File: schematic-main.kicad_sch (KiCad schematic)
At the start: 14 parts, among them J1 Conn_01x02, J2 Conn_01x03, J3 Conn_01x03_Pin, J6 Conn_01x04, P1 USB_C_Plug_USB2.0

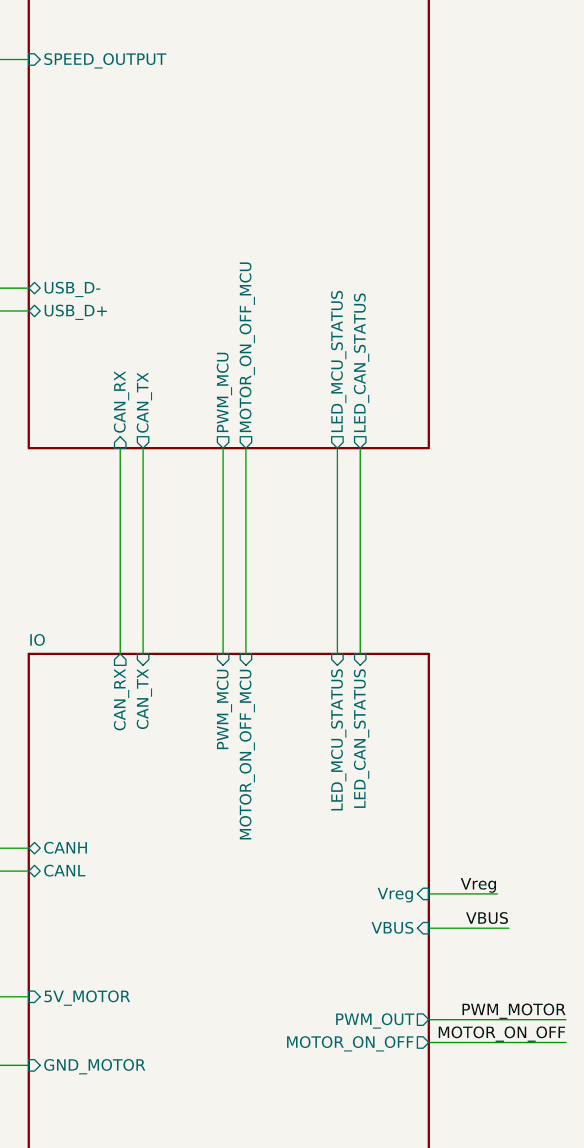
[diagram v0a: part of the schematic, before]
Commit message: Add test pins for I/O MCU
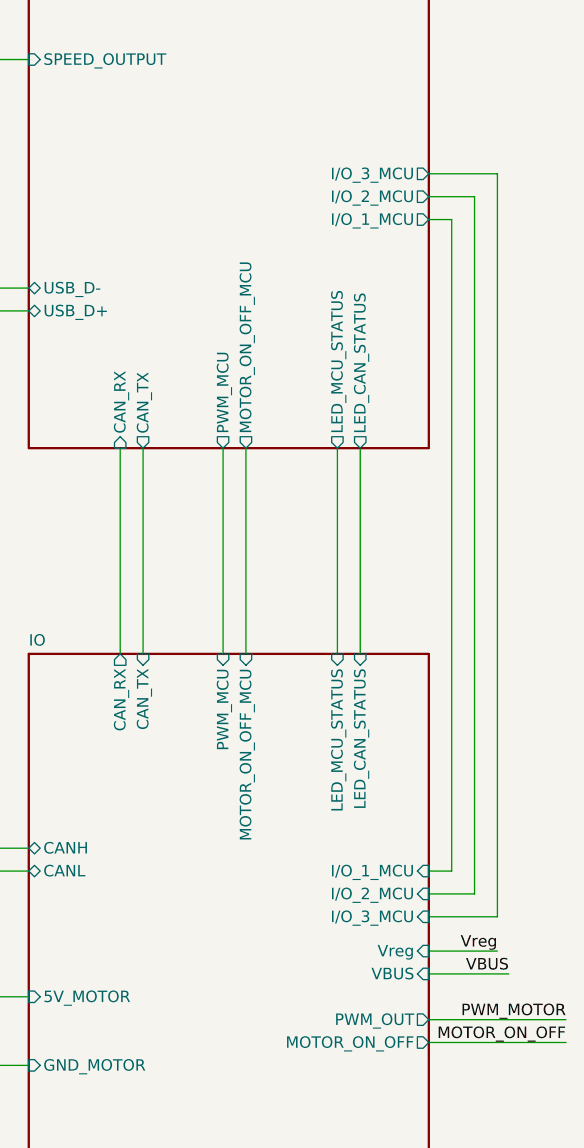
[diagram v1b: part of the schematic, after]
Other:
- sheet IO ports: added I/O_1_MCU, I/O_2_MCU, I/O_3_MCU; removed none
- sheet MCU ports: added I/O_1_MCU, I/O_2_MCU, I/O_3_MCU; removed none
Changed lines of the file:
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@@
     (stroke (width 0) (type default))
   )
-  (wire (pts (xy 179.07 134.62) (xy 187.96 134.62))
+  (wire (pts (xy 179.07 139.7) (xy 187.96 139.7))
+    (stroke (width 0) (type default))
+  )
+  (wire (pts (xy 179.07 130.81) (xy 184.15 130.81))
     (stroke (width 0) (type default))
   )
@@
     (stroke (width 0) (type default))
   )
+  (wire (pts (xy 186.69 50.8) (xy 186.69 133.35))
+    (stroke (width 0) (type default))
+  )
+  (wire (pts (xy 184.15 130.81) (xy 184.15 53.34))
+    (stroke (width 0) (type default))
+  )
   (wire (pts (xy 156.21 81.28) (xy 156.21 104.14))
     (stroke (width 0) (type default))
@@
     (stroke (width 0) (type default))
   )
-  (wire (pts (xy 179.07 130.81) (xy 186.69 130.81))
+  (wire (pts (xy 179.07 137.16) (xy 186.69 137.16))
     (stroke (width 0) (type default))
   )
@@
     (stroke (width 0) (type default))
   )
+  (wire (pts (xy 181.61 128.27) (xy 179.07 128.27))
+    (stroke (width 0) (type default))
+  )
   (wire (pts (xy 54.61 35.56) (xy 60.96 35.56))
     (stroke (width 0) (type default))
   )
+  (wire (pts (xy 179.07 53.34) (xy 184.15 53.34))
+    (stroke (width 0) (type default))
+  )
   (wire (pts (xy 130.81 147.32) (xy 115.57 147.32))
     (stroke (width 0) (type default))
@@
     (stroke (width 0) (type default))
   )
+  (wire (pts (xy 179.07 55.88) (xy 181.61 55.88))
+    (stroke (width 0) (type default))
+  )
+  (wire (pts (xy 179.07 50.8) (xy 186.69 50.8))
+    (stroke (width 0) (type default))
+  )
   (wire (pts (xy 124.46 63.5) (xy 134.62 63.5))
     (stroke (width 0) (type default))
@@
     (stroke (width 0) (type default))
   )
+  (wire (pts (xy 186.69 133.35) (xy 179.07 133.35))
+    (stroke (width 0) (type default))
+  )
   (wire (pts (xy 124.46 66.04) (xy 134.62 66.04))
+    (stroke (width 0) (type default))
+  )
+  (wire (pts (xy 181.61 55.88) (xy 181.61 128.27))
     (stroke (width 0) (type default))
   )
@@
     (effects (font (size 1.27 1.27)) (justify right bottom))
   )
-  (label "VBUS" (at 187.96 134.62 180) (fields_autoplaced)
+  (label "VBUS" (at 187.96 139.7 180) (fields_autoplaced)
     (effects (font (size 1.27 1.27)) (justify right bottom))
   )
@@
     (effects (font (size 1.27 1.27)) (justify right bottom))
   )
-  (label "Vreg" (at 186.69 130.81 180) (fields_autoplaced)
+  (label "Vreg" (at 186.69 137.16 180) (fields_autoplaced)
     (effects (font (size 1.27 1.27)) (justify right bottom))
   )
@@
       (effects (font (size 1.27 1.27)) (justify right))
     )
-    (pin "VBUS" input (at 179.07 134.62 0)
-      (effects (font (size 1.27 1.27)) (justify right))
-    )
-    (pin "Vreg" input (at 179.07 130.81 0)
+    (pin "VBUS" input (at 179.07 139.7 0)
+      (effects (font (size 1.27 1.27)) (justify right))
+    )
+    (pin "Vreg" input (at 179.07 137.16 0)
+      (effects (font (size 1.27 1.27)) (justify right))
+    )
+    (pin "I{slash}O_2_MCU" input (at 179.07 130.81 0)
+      (effects (font (size 1.27 1.27)) (justify right))
+    )
+    (pin "I{slash}O_1_MCU" input (at 179.07 128.27 0)
+      (effects (font (size 1.27 1.27)) (justify right))
+    )
+    (pin "I{slash}O_3_MCU" input (at 179.07 133.35 0)
       (effects (font (size 1.27 1.27)) (justify right))
     )
@@
       (effects (font (size 1.27 1.27)) (justify left))
     )
-    (instances
+    (pin "I{slash}O_1_MCU" output (at 179.07 55.88 0)
+      (effects (font (size 1.27 1.27)) (justify right))
+    )
+    (pin "I{slash}O_2_MCU" output (at 179.07 53.34 0)
+      (effects (font (size 1.27 1.27)) (justify right))
+    )
+    (pin "I{slash}O_3_MCU" output (at 179.07 50.8 0)
+      (effects (font (size 1.27 1.27)) (justify right))
+    )
+    (instances

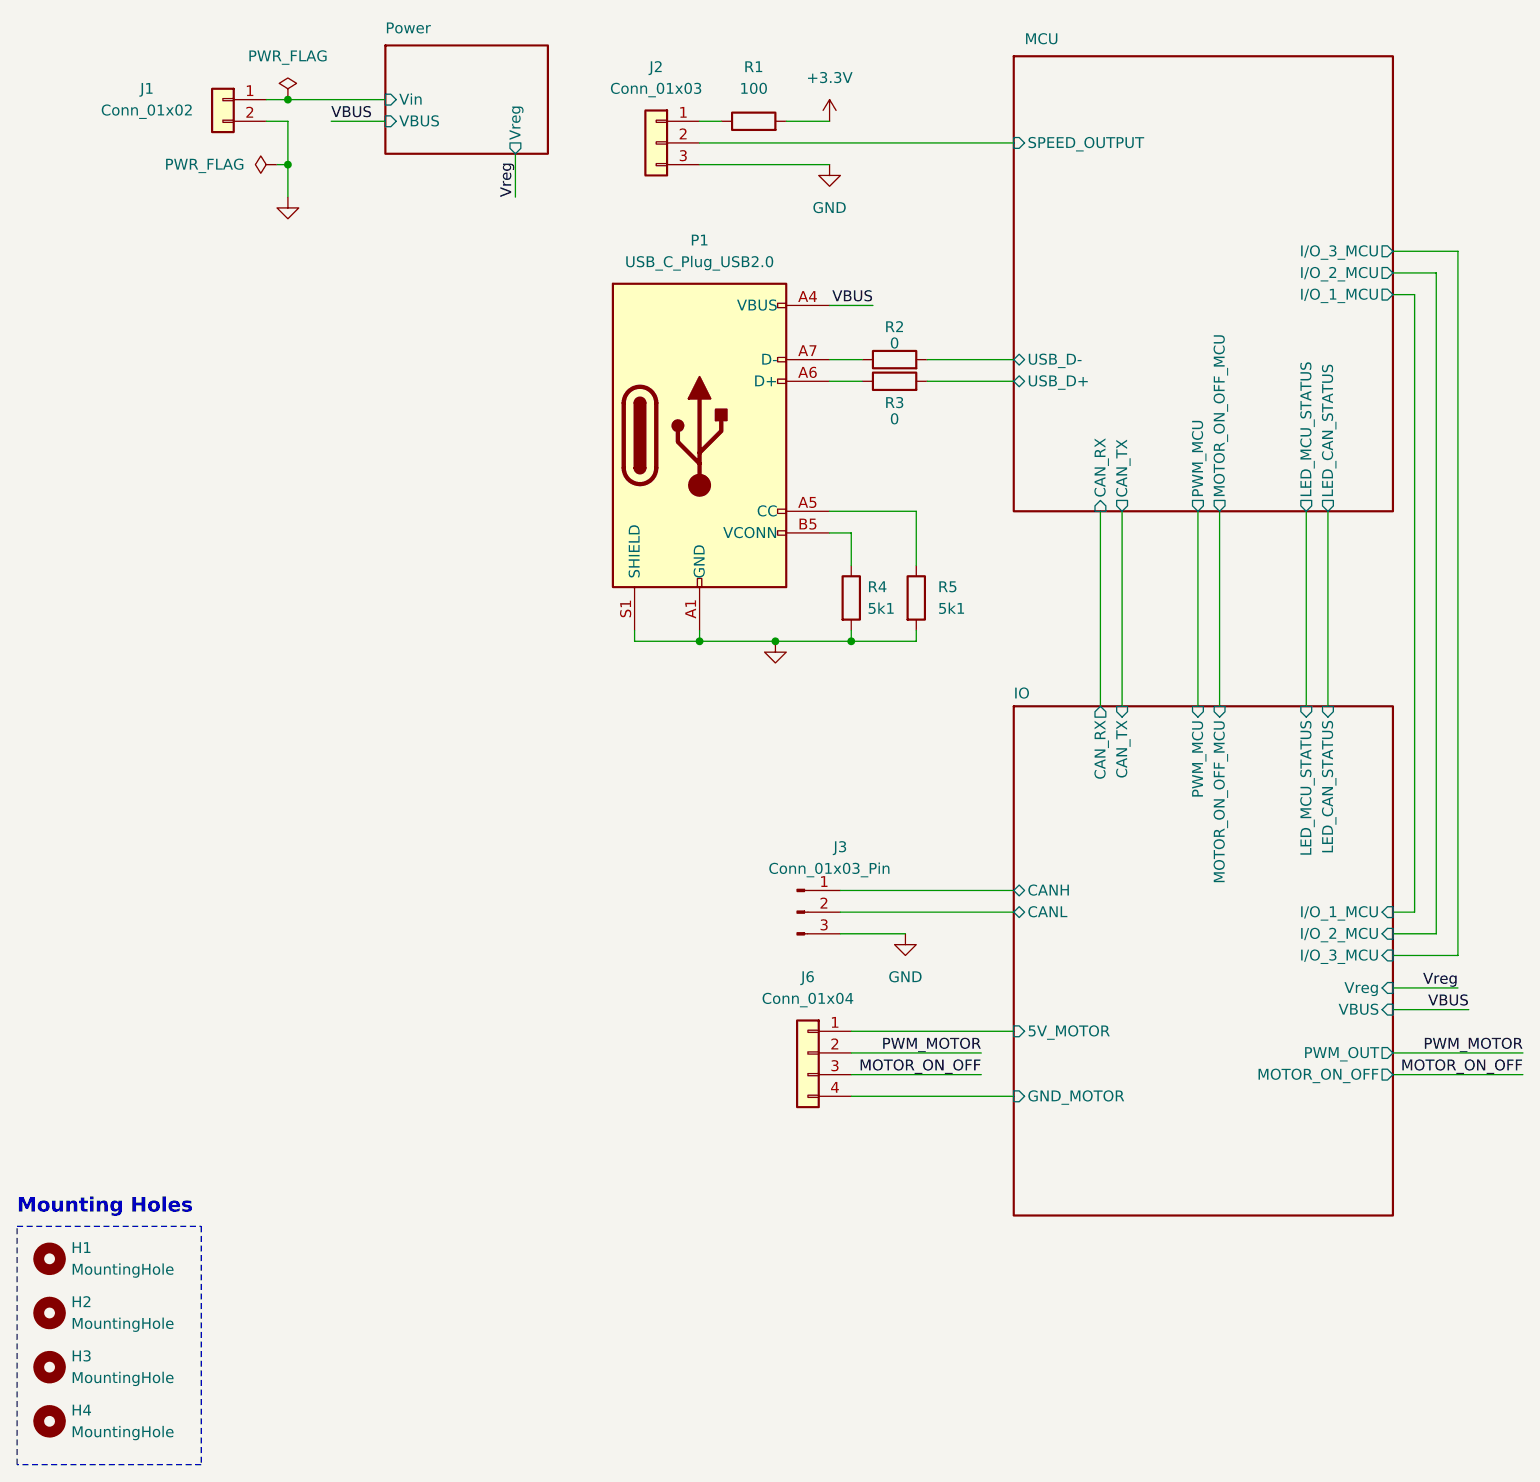
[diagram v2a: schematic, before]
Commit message: Add Emergency button option
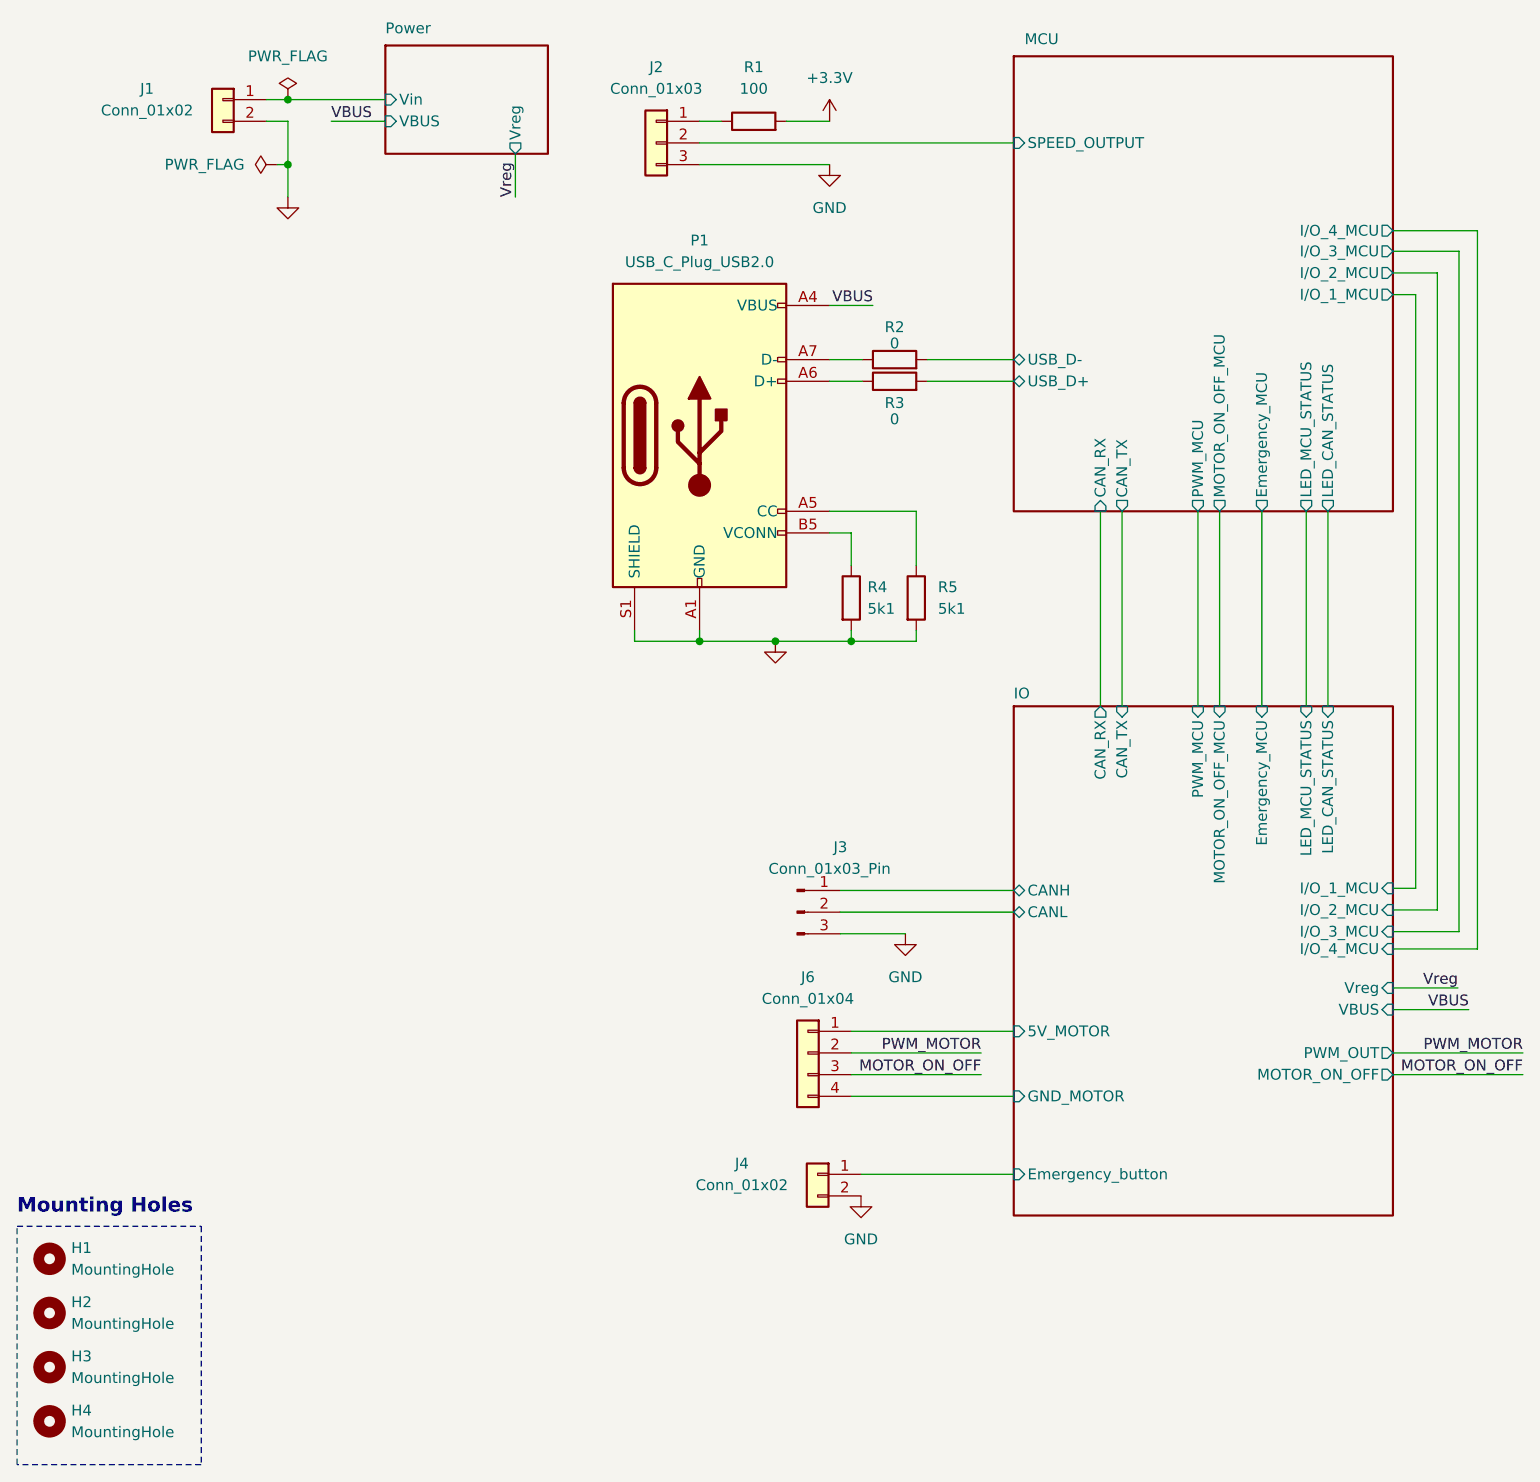
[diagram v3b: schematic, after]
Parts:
- added J4: Conn_01x02, Connector_Molex:39-30-102Y, symbol Connector_Generic:Conn_01x02
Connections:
- net GND: now also J4.2 (Pin_2)
- new net IO/Emergency_button: J4.1 (Pin_1)
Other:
- sheet IO ports: added Emergency_MCU, Emergency_button, I/O_4_MCU; removed none
- sheet MCU ports: added Emergency_MCU, I/O_4_MCU; removed none
